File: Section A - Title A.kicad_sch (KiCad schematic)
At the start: 0 parts

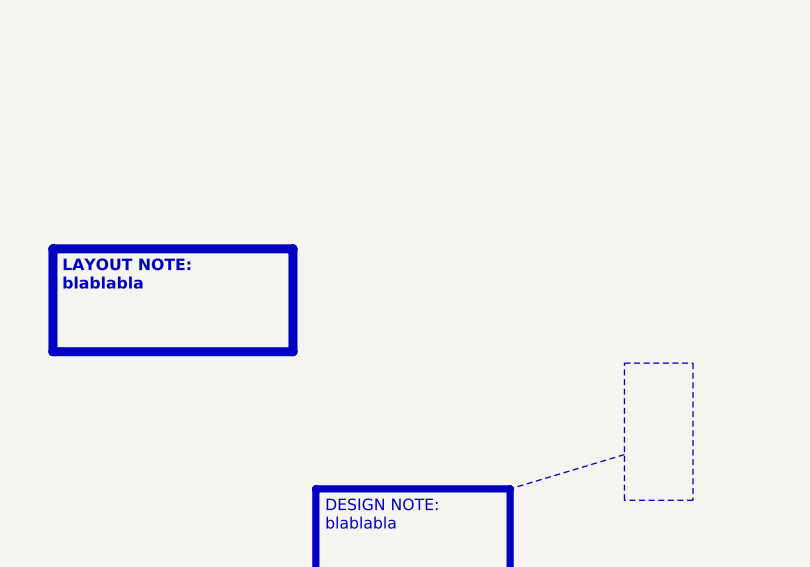
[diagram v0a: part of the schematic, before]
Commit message: section-a: add R301 10k
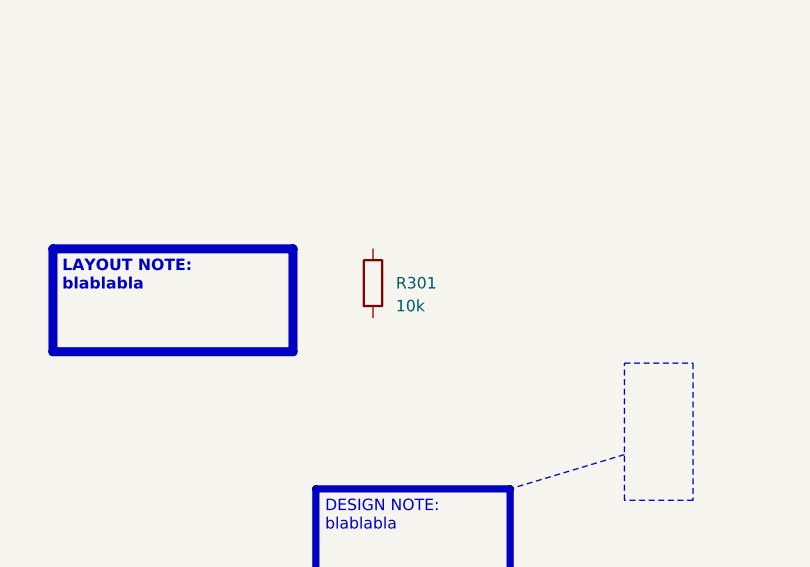
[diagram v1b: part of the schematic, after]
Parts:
- added R301: 10k, Resistor_SMD:R_0603_1608Metric, symbol Device:R
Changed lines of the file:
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@@
+		)
+	)
+	(symbol
+		(lib_id "Device:R")
+		(at 101.6 101.6 0)
+		(unit 1)
+		(exclude_from_sim no)
+		(in_bom yes)
+		(on_board yes)
+		(dnp no)
+		(property "Reference" "R301"
+			(at 104.14 101.6 0)
+			(effects (font (size 1.27 1.27)) (justify left))
+		)
+		(property "Value" "10k"
+			(at 104.14 104.14 0)
+			(effects (font (size 1.27 1.27)) (justify left))
+		)
+		(property "Footprint" "Resistor_SMD:R_0603_1608Metric"
+			(at 101.6 101.6 0)
+			(effects (font (size 1.27 1.27)) (hide yes))
+		)
+		(property "Datasheet" "~"
+			(at 101.6 101.6 0)
+			(effects (font (size 1.27 1.27)) (hide yes))
+		)
+		(pin "1")
+		(pin "2")
+		(instances
+			(project "ci_dummy"
+				(path "/f9e05184-c88b-4a88-ae9c-ab2bdb32be7c/c5103ceb-5325-4a84-a025-9638a412984e/f06537ee-772d-44d3-8c50-e0ba41038c9c"
+					(reference "R301")
+					(unit 1)
+				)
+			)
 		)
 	)

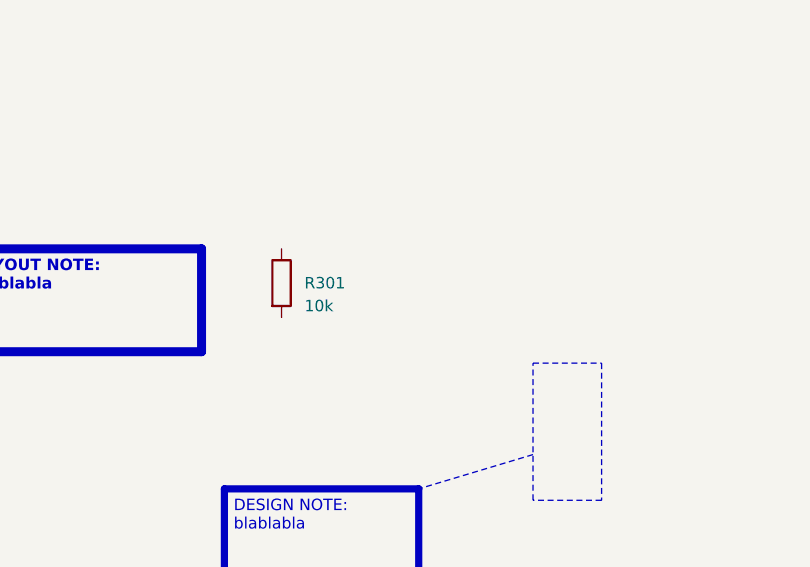
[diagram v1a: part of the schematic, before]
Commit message: section-a: add R302 22k
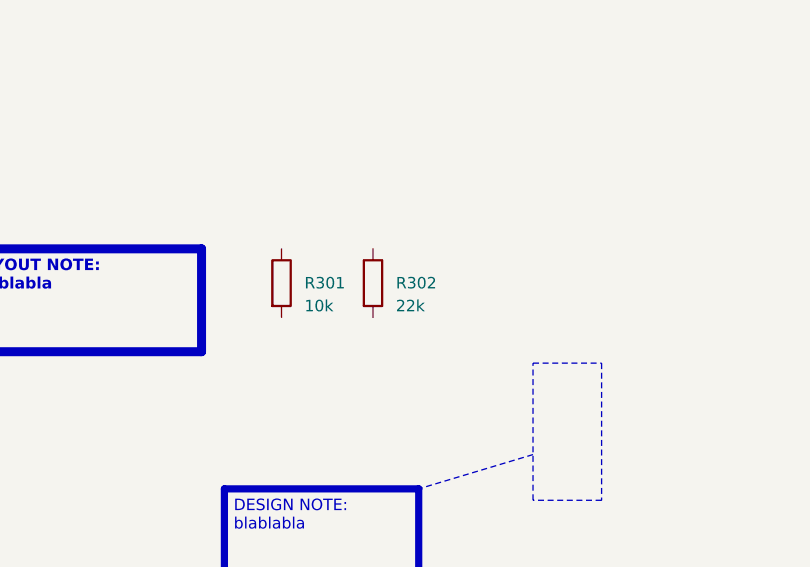
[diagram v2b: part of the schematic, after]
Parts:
- added R302: 22k, Resistor_SMD:R_0603_1608Metric, symbol Device:R
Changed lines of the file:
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@@
+		)
+	)
+	(symbol
+		(lib_id "Device:R")
+		(at 111.76 101.6 0)
+		(unit 1)
+		(exclude_from_sim no)
+		(in_bom yes)
+		(on_board yes)
+		(dnp no)
+		(property "Reference" "R302"
+			(at 114.30000000000001 101.6 0)
+			(effects (font (size 1.27 1.27)) (justify left))
+		)
+		(property "Value" "22k"
+			(at 114.30000000000001 104.14 0)
+			(effects (font (size 1.27 1.27)) (justify left))
+		)
+		(property "Footprint" "Resistor_SMD:R_0603_1608Metric"
+			(at 111.76 101.6 0)
+			(effects (font (size 1.27 1.27)) (hide yes))
+		)
+		(property "Datasheet" "~"
+			(at 111.76 101.6 0)
+			(effects (font (size 1.27 1.27)) (hide yes))
+		)
+		(pin "1")
+		(pin "2")
+		(instances
+			(project "ci_dummy"
+				(path "/f9e05184-c88b-4a88-ae9c-ab2bdb32be7c/c5103ceb-5325-4a84-a025-9638a412984e/f06537ee-772d-44d3-8c50-e0ba41038c9c"
+					(reference "R302")
+					(unit 1)
+				)
+			)
 		)
 	)

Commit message: feature/section-a: add R1 (annotated entire schematic)
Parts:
- added R1: 2k2, Resistor_SMD:R_0603_1608Metric, symbol Device:R
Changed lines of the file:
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@@
+		)
+	)
+	(symbol
+		(lib_id "Device:R")
+		(at 121.92 101.6 0)
+		(unit 1)
+		(exclude_from_sim no)
+		(in_bom yes)
+		(on_board yes)
+		(dnp no)
+		(property "Reference" "R1"
+			(at 124.46000000000001 101.6 0)
+			(effects (font (size 1.27 1.27)) (justify left))
+		)
+		(property "Value" "2k2"
+			(at 124.46000000000001 104.14 0)
+			(effects (font (size 1.27 1.27)) (justify left))
+		)
+		(property "Footprint" "Resistor_SMD:R_0603_1608Metric"
+			(at 121.92 101.6 0)
+			(effects (font (size 1.27 1.27)) (hide yes))
+		)
+		(property "Datasheet" "~"
+			(at 121.92 101.6 0)
+			(effects (font (size 1.27 1.27)) (hide yes))
+		)
+		(pin "1")
+		(pin "2")
+		(instances
+			(project "ci_dummy"
+				(path "/f9e05184-c88b-4a88-ae9c-ab2bdb32be7c/c5103ceb-5325-4a84-a025-9638a412984e/f06537ee-772d-44d3-8c50-e0ba41038c9c"
+					(reference "R1")
+					(unit 1)
+				)
+			)
 		)
 	)

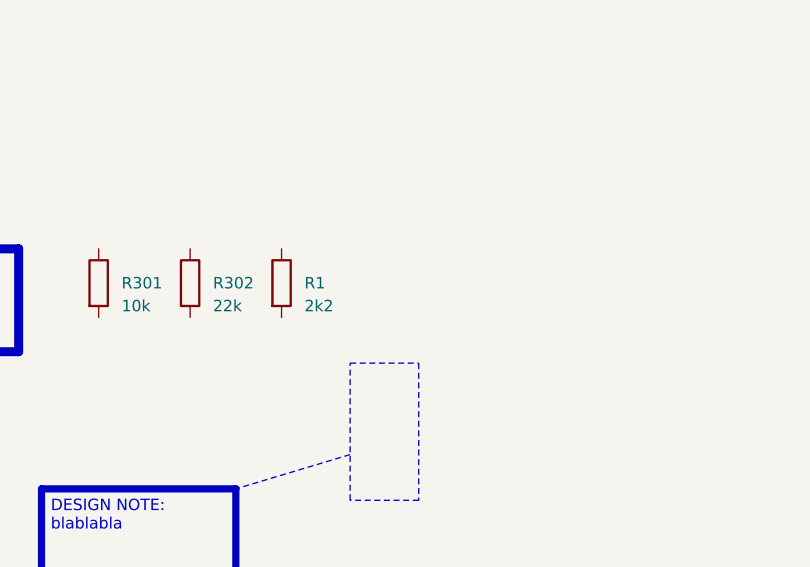
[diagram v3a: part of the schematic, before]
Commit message: section-a: add R303 (unconnected)
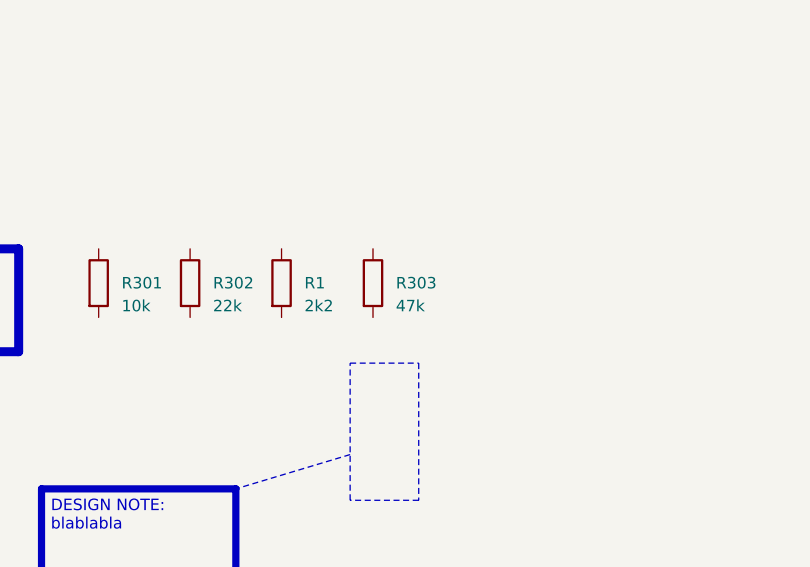
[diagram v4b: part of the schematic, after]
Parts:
- added R303: 47k, Resistor_SMD:R_0603_1608Metric, symbol Device:R
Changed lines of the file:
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@@
+		)
+	)
+	(symbol
+		(lib_id "Device:R")
+		(at 132.08 101.6 0)
+		(unit 1)
+		(exclude_from_sim no)
+		(in_bom yes)
+		(on_board yes)
+		(dnp no)
+		(property "Reference" "R303"
+			(at 134.62 101.6 0)
+			(effects (font (size 1.27 1.27)) (justify left))
+		)
+		(property "Value" "47k"
+			(at 134.62 104.14 0)
+			(effects (font (size 1.27 1.27)) (justify left))
+		)
+		(property "Footprint" "Resistor_SMD:R_0603_1608Metric"
+			(at 132.08 101.6 0)
+			(effects (font (size 1.27 1.27)) (hide yes))
+		)
+		(property "Datasheet" "~"
+			(at 132.08 101.6 0)
+			(effects (font (size 1.27 1.27)) (hide yes))
+		)
+		(pin "1")
+		(pin "2")
+		(instances
+			(project "ci_dummy"
+				(path "/f9e05184-c88b-4a88-ae9c-ab2bdb32be7c/c5103ceb-5325-4a84-a025-9638a412984e/f06537ee-772d-44d3-8c50-e0ba41038c9c"
+					(reference "R303")
+					(unit 1)
+				)
+			)
 		)
 	)
